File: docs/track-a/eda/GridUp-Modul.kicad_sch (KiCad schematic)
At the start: 47 parts, among them J1 İç ihtiyaç L / N / PE, J2 CT L1, J3 CT L2, J4 CT L3, J5 CT nötr, J6 Genişleme 2×5, J7 RS-485 klemens A / GND / B, J8 SMA panel, J9 Servis USB/UART0, SW1 Reset, U1 ESP32-S3-WROOM-1U-N8, U2 MLX90640ESF-BAA, U3 SHT31-DIS-B, U4 MAX3485, U5 RAC05-05SK/277, U6 LDO 3,3 V ≥600 mA (LD1117S33)

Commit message: İZ A: 03-baglanti-semasi.svg artık KiCad şematiğinden üretiliyor (elle SVG kaldırıldı): sinyal akışına göre yerleşim (CT üst / I²C alt → ESP32 → servis / RS-485 / anten / genişleme; besleme altta), ana hatlar tel (I²C bus, CT merdiveni, UART1↔MAX3485 aynalı), net renk kodu + lejant + blok dolguları, çerçevesiz kırpılmış SVG (2,0 mm etiket ≈ 8 px @1200 px); ERC 0/0, netlist 95 kontrol; 03-pinout ve eda/README güncel
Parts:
- removed C10, C11, C12, C13, C2: 100 nF, symbol Device:C
- removed D1: Schottky (OR), symbol Device:D_Schottky
- removed J7: RS-485 klemens A / GND / B, TerminalBlock_Phoenix:TerminalBlock_Phoenix_MKDS-3-3-5.08_1x03_P5.08mm_Horizontal, symbol Connector_Generic:Conn_01x03
- removed R40: 120 Ω, symbol Device:R
- removed RV1: MOV, symbol Device:Varistor
- removed U6: LDO 3,3 V ≥600 mA (LD1117S33), Package_TO_SOT_SMD:SOT-223-3_TabPin2, symbol Regulator_Linear:LD1117S33TR_SOT223
- added C31: 10 µF, symbol Device:C
- added C32: C_sc süperkap., symbol Device:C_Polarized
- added F1: sigorta, symbol Device:Fuse
- added J1: İç ihtiyaç L / N / PE, TerminalBlock_Phoenix:TerminalBlock_Phoenix_MKDS-3-3-5.08_1x03_P5.08mm_Horizontal, symbol Connector_Generic:Conn_01x03
- added J2: CT L1, TerminalBlock_Phoenix:TerminalBlock_Phoenix_MKDS-3-2-5.08_1x02_P5.08mm_Horizontal, symbol Connector_Generic:Conn_01x02
- added J3: CT L2, TerminalBlock_Phoenix:TerminalBlock_Phoenix_MKDS-3-2-5.08_1x02_P5.08mm_Horizontal, symbol Connector_Generic:Conn_01x02
- added J4: CT L3, TerminalBlock_Phoenix:TerminalBlock_Phoenix_MKDS-3-2-5.08_1x02_P5.08mm_Horizontal, symbol Connector_Generic:Conn_01x02
- added J5: CT nötr, TerminalBlock_Phoenix:TerminalBlock_Phoenix_MKDS-3-2-5.08_1x02_P5.08mm_Horizontal, symbol Connector_Generic:Conn_01x02
- added R52: R_şarj ≈10 Ω, symbol Device:R
- added U4: MAX3485, Package_SO:SOIC-8_3.9x4.9mm_P1.27mm, symbol Interface_UART:MAX3485
- C10: renamed from J2; value CT L1 -> 100 nF; footprint TerminalBlock_Phoenix:TerminalBlock_Phoenix_MKDS-3-2-5.08_1x02_P5.08mm_Horizontal -> (none); symbol Connector_Generic:Conn_01x02 -> Device:C
- C11: renamed from J3; value CT L2 -> 100 nF; footprint TerminalBlock_Phoenix:TerminalBlock_Phoenix_MKDS-3-2-5.08_1x02_P5.08mm_Horizontal -> (none); symbol Connector_Generic:Conn_01x02 -> Device:C
- C12: renamed from J4; value CT L3 -> 100 nF; footprint TerminalBlock_Phoenix:TerminalBlock_Phoenix_MKDS-3-2-5.08_1x02_P5.08mm_Horizontal -> (none); symbol Connector_Generic:Conn_01x02 -> Device:C
- C13: renamed from J5; value CT nötr -> 100 nF; footprint TerminalBlock_Phoenix:TerminalBlock_Phoenix_MKDS-3-2-5.08_1x02_P5.08mm_Horizontal -> (none); symbol Connector_Generic:Conn_01x02 -> Device:C
- C2: renamed from U4; value MAX3485 -> 100 nF; footprint Package_SO:SOIC-8_3.9x4.9mm_P1.27mm -> (none); symbol Interface_UART:MAX3485 -> Device:C
- D1: renamed from R52; value R_şarj ≈10 Ω -> Schottky (OR); symbol Device:R -> Device:D_Schottky
- J7: renamed from J1; value İç ihtiyaç L / N / PE -> RS-485 klemens B / GND / A
- R40: renamed from F1; value sigorta -> 120 Ω; symbol Device:Fuse -> Device:R
- RV1: renamed from C31; value 10 µF -> MOV; symbol Device:C -> Device:Varistor
- U6: renamed from C32; value C_sc süperkap. -> LD1117S33 — 3,3 V, ≥600 mA; footprint (none) -> Package_TO_SOT_SMD:SOT-223-3_TabPin2; symbol Device:C_Polarized -> Regulator_Linear:LD1117S33TR_SOT223
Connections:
- net +3V3: now also C2.1, U6.2 (VO), C31.1, U4.8 (VCC); no longer C2.8 (VCC), RV1.1
- net +5V: now also U6.3 (VI), R52.1
- net 5V_RAW: now also D1.2 (A)
- net CT_L1: now also C10.1
- net CT_L2: now also C11.1
- net CT_L3: now also C12.1
- net CT_N: now also C13.1
- net DE_RE: now also U4.2 (~{RE}), U4.3 (DE); no longer C2.2 (~{RE}), C2.3 (DE)
- net Earth_Protective: now also J1.3 (Pin_3); no longer J7.3 (Pin_3)
- net GND: now also C10.2, C11.2, C12.2, C13.2, C2.2, J7.2 (Pin_2), U6.1 (GND), C31.2, C32.2, U4.5 (GND); no longer C2.5 (GND), RV1.2, U6.2
- net U0RXD: now also J9.2 (Pin_2); no longer J9.4 (Pin_4)
- net U0TXD: now also J9.1 (Pin_1); no longer J9.3 (Pin_3)
- net U1RXD: now also U4.1 (RO); no longer C2.1 (RO)
- net U1TXD: now also U4.4 (DI); no longer C2.4 (DI)
- net USB_DN: now also J9.3 (Pin_3); no longer J9.1 (Pin_1)
- net USB_DP: now also J9.4 (Pin_4); no longer J9.2 (Pin_2)
- net V_BIAS: now also J2.2 (Pin_2), J3.2 (Pin_2), J4.2 (Pin_2), J5.2 (Pin_2); no longer C10.2 (Pin_2), C11.2 (Pin_2), C12.2 (Pin_2), C13.2 (Pin_2)
- net at R40.2: now also J7.3 (Pin_3), U4.6 (A); no longer U5.1 (AC(L))
- net at U5.2 (AC(N)): now also RV1.2, J1.2 (Pin_2); no longer J7.2 (Pin_2)
- net at R10.1, R20.1: now also J2.1 (Pin_1); no longer C10.1 (Pin_1)
- net at R11.1, R21.1: now also J3.1 (Pin_1); no longer C11.1 (Pin_1)
- net at R12.1, R22.1: now also J4.1 (Pin_1); no longer C12.1 (Pin_1)
- net at J7.1 (Pin_1), R40.1: now also U4.7 (B)
- net at R13.1, R23.1: now also J5.1 (Pin_1); no longer C13.1 (Pin_1)
- new net: C32.1, D2.2 (A), R52.2
- new net: F1.1, J1.1 (Pin_1)
- new net: F1.2, RV1.1, U5.1 (AC(L))
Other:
- note added: "2× 4,7 kΩ pull-up → 3V3"
- note added: "3V3"
- note added: "5 V / 230 V"
- note added: "A/B bükümlü çift, ekranlı; son cihazda 2. 120 Ω"
- note added: "Anten — U.FL pigtail → SMA panel → dış anten (pano dış yüzü)"
- note added: "Besleme — 230 V iç ihtiyaç → RAC05 5 V → D1 (OR) → 5 V rayı → LDO 3V3; süperkap R_şarj + D2 yedek; algılama D1 öncesi (§3.4, §7.3)"
- note added: "CT ×4 (analizör yoksa) — burden, V_bias, RC → ADC1"
- note added: "ESP32-S3-WROOM-1U-N8 — Wi-Fi/BLE, U.FL anten"
- note added: "GND / PE"
- note added: "Genişleme 2×5 (boş) — PD / akustik için ayrılmış (§7.1); kör tapa"
- note added: "I²C"
- note added: "I²C — MLX90640 0x33 + SHT31 0x44, tek hat 400 kHz+"
- note added: "KiCad şematik (eda/GridUp-Modul.kicad_sch): ERC 0 hata / 0 uyarı, netlist §3.1 tablosuyla otomatik doğrulanmış. Kavramsal — üretim çizimi değildir (§1.4); pasif değerler tipik."
- note added: "Lejant (tel / etiket rengi) — aynı adlı etiketler aynı nettir; tel kesişmeleri atlama yayıyla gösterilir (bağlantı yok):"
- note added: "Modül bağlantı şeması — ESP32-S3-WROOM-1U etrafında (03-pinout §3.1–3.6)"
- note added: "RS-485 / Modbus RTU — MAX3485, 3,3 V, yarıçift; 120 Ω sonlandırma"
- note added: "U.FL harici anten (1U) — sembolde pin yok, bkz. J8; GPIO10/11 → genişleme (J6)"
- note added: "U.FL pigtail (modül konnektörü) — RF, şemada net değil; mevcut kablo girişinden"
- note added: "UART / RS-485"
- note added: "V_bias = 3V3/2 (CT ön yargı)"
- note added: "analog (CT, algılama)"
- note added: "diğer / bileşen içi"
- note added: "strapping IO0 / IO3 / IO45 / IO46 bağlanmaz; IO35–IO37 flash — kullanılmaz"
- note added: "sıcaklık + nem (ADDR → GND: 0x44)"
- note added: "termal dizi 32×24, 110°×75°, ≤23 mA"
- note added: "→ enerji analizörü (slave 1, akım) / TVOC-2 (slave 2, yalnız trip-diag.)"
- note removed: "Anten — U.FL pigtail → SMA panel konnektörü → dış anten (pano dış yüzü, mevcut kablo girişi)"
- note removed: "Besleme — 230 V iç ihtiyaç devresi → RAC05 5 V → D1 (OR) → 5 V rayı → LDO 3V3; süperkap R_şarj + D2 yedek; algılama D1 öncesinden (03 §3.4, §7.3)"
- note removed: "Genişleme başlığı 2×5 (boş) — PD / akustik için ayrılmış, §7.1 şartı; kutuda kör tapa"
- note removed: "I²C — tek hat, 400 kHz+, 0x33 ≠ 0x44, 2× 4,7 kΩ pull-up → 3V3"
- note removed: "RS-485 / Modbus RTU — MAX3485 sınıfı, 3,3 V, yarıçift yönlü; 120 Ω sonlandırma; A/B bükümlü çift, ekranlı"
- note removed: "Split-core CT ×4 (analizör yoksa) — L1 / L2 / L3 / nötr, her kanal aynı devre: burden + V_bias, 1 kΩ / 100 nF RC → ADC1"
- note removed: "U.FL harici anten (1U) — sembolde pin yok, bkz. J8"
- note removed: "U.FL pigtail (modül konnektörü) — RF, şemada net değil"
- note removed: "V_bias = 3V3/2"
- note removed: "son cihazda 2. 120 Ω sonlandırma"
- note removed: "strapping: IO0 / IO3 / IO45 / IO46 — bağlanmaz; IO35–IO37 flash — kullanılmaz"
- note removed: "sıcaklık + nem, I²C 0x44 (ADDR → GND)"
- note removed: "termal dizi 32×24, 110°×75°, I²C 0x33"
- note removed: "→ enerji analizörü (slave 1, akım) / TVOC-2 (slave 2, yalnız trip-diag. kaydı)"
- note removed: "≤23 mA, 3,3 V"
- moved on the sheet: J7

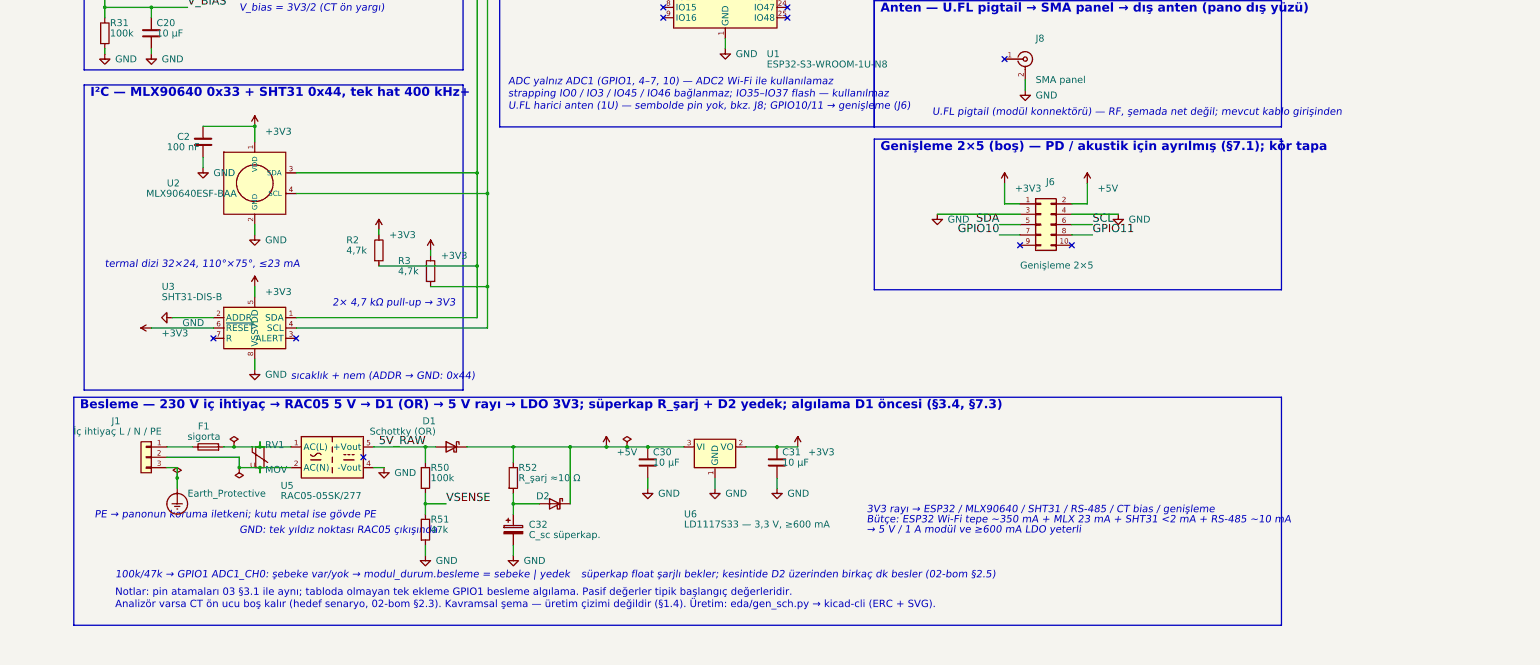
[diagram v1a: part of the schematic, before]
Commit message: İZ A: model/şema datasheet düzeltmeleri — RAC05-05SK/277 31,7 × 26,7 × 21,8 (LDO/D1/D2/bölücü kaydırıldı); süperkap 2× Eaton HV1030-2R7106-R (Ø10,5 × 31,5, 10 F / 2,7 V seri, 10 k dengeleme) + TPS61099 boost 4,6 V → D2 (LD1117 yerine AP7361C-33E düşük dropout); kutu alt yüz rakor sırası PCB klemensleriyle hizalı (RS-485 / SMA / CT / 230 V, PG7 Ø12,5); 02/03/04 SVG'ler, views, f3d/step yeniden üretildi; ERC 0/0, netlist 103 kontrol; README/03-pinout senkron
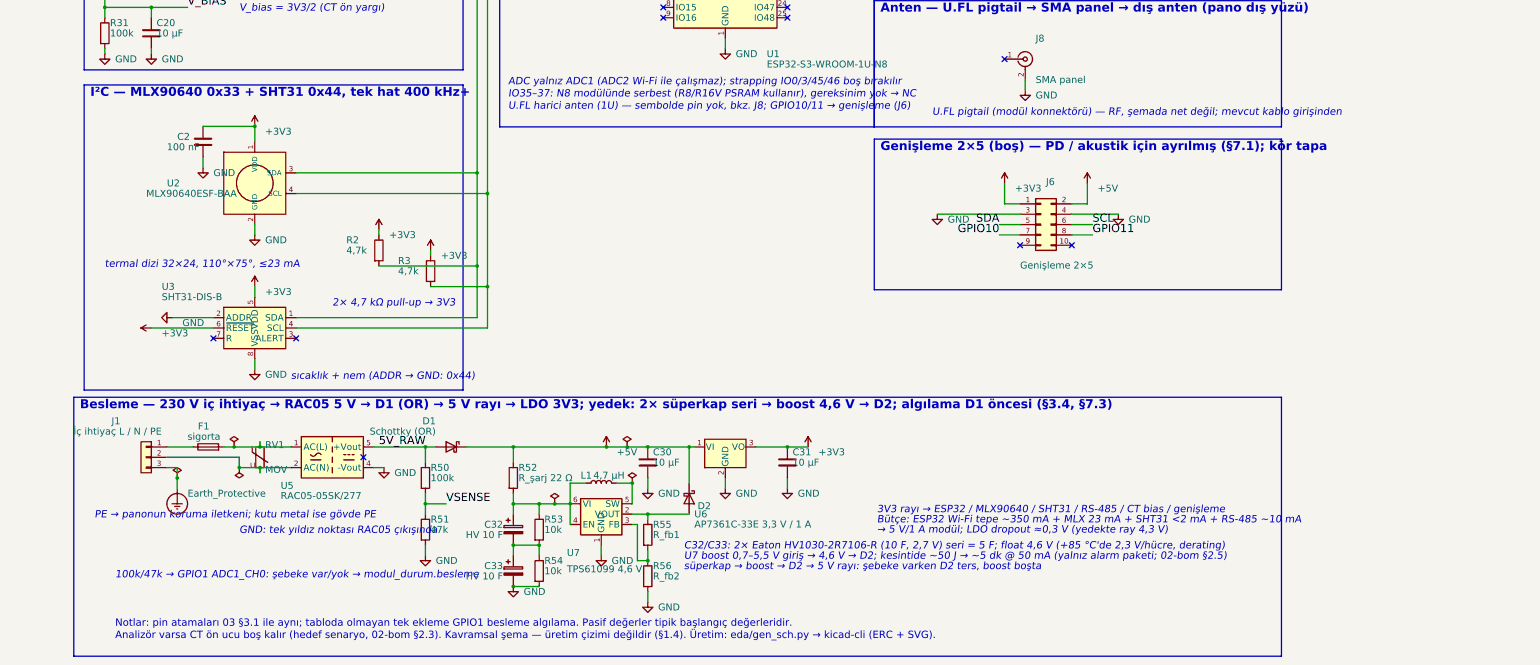
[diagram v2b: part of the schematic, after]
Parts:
- removed C12, C13: 100 nF, symbol Device:C
- removed J5: CT nötr, TerminalBlock_Phoenix:TerminalBlock_Phoenix_MKDS-3-2-5.08_1x02_P5.08mm_Horizontal, symbol Connector_Generic:Conn_01x02
- removed R1: 10k, symbol Device:R
- removed R30: 100k, symbol Device:R
- removed R40: 120 Ω, symbol Device:R
- added C2: 100 nF, symbol Device:C
- added C20: 10 µF, symbol Device:C
- added C33: HV 10 F, symbol Device:C_Polarized
- added J3: CT L2, TerminalBlock_Phoenix:TerminalBlock_Phoenix_MKDS-3-2-5.08_1x02_P5.08mm_Horizontal, symbol Connector_Generic:Conn_01x02
- added L1: 4,7 µH, symbol Device:L
- added R53, R54: 10k, symbol Device:R
- added R55: R_fb1, symbol Device:R
- added R56: R_fb2, symbol Device:R
- added U2: MLX90640ESF-BAA, Package_TO_SOT_THT:TO-39-4, symbol GridUp:MLX90640
- added U3: SHT31-DIS-B, Sensor_Humidity:Sensirion_DFN-8-1EP_2.5x2.5mm_P0.5mm_EP1.1x1.7mm, symbol Sensor_Humidity:SHT31-DIS
- added U6: AP7361C-33E 3,3 V / 1 A, Package_TO_SOT_SMD:SOT-223-3_TabPin2, symbol Regulator_Linear:AP7361C-33E
- added U7: TPS61099 4,6 V, Package_SON:WSON-6-1EP_2x2mm_P0.65mm_EP1x1.6mm, symbol Regulator_Switching:TPS61099DRV
- C12: renamed from C20; value 10 µF -> 100 nF
- C32: value C_sc süperkap. -> HV 10 F
- J1: renamed from U6; value LD1117S33 — 3,3 V, ≥600 mA -> İç ihtiyaç L / N / PE; footprint Package_TO_SOT_SMD:SOT-223-3_TabPin2 -> TerminalBlock_Phoenix:TerminalBlock_Phoenix_MKDS-3-3-5.08_1x03_P5.08mm_Horizontal; symbol Regulator_Linear:LD1117S33TR_SOT223 -> Connector_Generic:Conn_01x03
- J5: renamed from U2; value MLX90640ESF-BAA -> CT nötr; footprint Package_TO_SOT_THT:TO-39-4 -> TerminalBlock_Phoenix:TerminalBlock_Phoenix_MKDS-3-2-5.08_1x02_P5.08mm_Horizontal; symbol GridUp:MLX90640 -> Connector_Generic:Conn_01x02
- R1: renamed from J3; value CT L2 -> 10k; footprint TerminalBlock_Phoenix:TerminalBlock_Phoenix_MKDS-3-2-5.08_1x02_P5.08mm_Horizontal -> (none); symbol Connector_Generic:Conn_01x02 -> Device:R
- R30: renamed from U3; value SHT31-DIS-B -> 100k; footprint Sensor_Humidity:Sensirion_DFN-8-1EP_2.5x2.5mm_P0.5mm_EP1.1x1.7mm -> (none); symbol Sensor_Humidity:SHT31-DIS -> Device:R
- R40: renamed from J1; value İç ihtiyaç L / N / PE -> 120 Ω; footprint TerminalBlock_Phoenix:TerminalBlock_Phoenix_MKDS-3-3-5.08_1x03_P5.08mm_Horizontal -> (none); symbol Connector_Generic:Conn_01x03 -> Device:R
- R52: value R_şarj ≈10 Ω -> R_şarj 22 Ω
- renumbered C2 to C13
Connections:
- net +3V3: now also R1.1, R30.1, C2.1, U2.1 (VDD), U3.5 (VDD), U3.6 (~{RESET}), U6.3 (VO); no longer C13.1, J1.2 (VO), J5.1 (VDD), R30.5 (VDD), R30.6 (~{RESET})
- net +5V: now also U6.1 (VI); no longer J1.3 (VI)
- net CT_L3: now also C12.1
- net CT_N: now also C13.1
- net Earth_Protective: now also J1.3 (Pin_3); no longer R40.3 (Pin_3)
- net GND: now also C2.2, C20.2, C33.2, R54.2, R56.2, U2.2 (GND), U3.2 (ADDR), U3.8 (VSS), U3.9 (VSS), U6.2 (GND), U7.1 (GND), U7.7 (GND); no longer C32.2, J1.1 (GND), J5.2 (GND), R30.2 (ADDR), R30.8 (VSS), R30.9 (VSS)
- net SCL: now also U2.4 (SCL), U3.4 (SCL); no longer J5.4 (SCL), R30.4 (SCL)
- net SDA: now also U2.3 (SDA), U3.1 (SDA); no longer J5.3 (SDA), R30.1 (SDA)
- net V_BIAS: now also J5.2 (Pin_2), R30.2, C20.1, J3.2 (Pin_2); no longer C12.1, R1.2 (Pin_2)
- net at R13.1, R23.1: now also J5.1 (Pin_1)
- net at C1.1, SW1.2, U1.3 (EN): now also R1.2
- net at C32.1, R52.2: now also L1.1, R53.1, U7.4 (EN), U7.6 (VI); no longer D2.2 (A)
- net at J7.1 (Pin_1), U4.7 (B): now also R40.1
- net at J7.3 (Pin_3), U4.6 (A): now also R40.2
- net at F1.1: now also J1.1 (Pin_1); no longer R40.1 (Pin_1)
- net at RV1.2, U5.2 (AC(N)): now also J1.2 (Pin_2); no longer R40.2 (Pin_2)
- net at R11.1, R21.1: now also J3.1 (Pin_1); no longer R1.1 (Pin_1)
- new net: D2.2 (A), R55.1, U7.2 (VOUT)
- new net: R55.2, R56.1, U7.3 (FB)
- new net: C32.2, C33.1, R53.2, R54.1
- new net: L1.2, U7.5 (SW)
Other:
- note added: "100k/47k → GPIO1 ADC1_CH0: şebeke var/yok → modul_durum.besleme"
- note added: "ADC yalnız ADC1 (ADC2 Wi-Fi ile çalışmaz); strapping IO0/3/45/46 boş bırakılır"
- note added: "Besleme — 230 V iç ihtiyaç → RAC05 5 V → D1 (OR) → 5 V rayı → LDO 3V3; yedek: 2× süperkap seri → boost 4,6 V → D2; algılama D1 öncesi (§3.4, §7.3)"
- note added: "C32/C33: 2× Eaton HV1030-2R7106-R (10 F, 2,7 V) seri = 5 F; float 4,6 V (+85 °C'de 2,3 V/hücre, derating)"
- note added: "IO35–37: N8 modülünde serbest (R8/R16V PSRAM kullanır), gereksinim yok → NC"
- note added: "U7 boost 0,7–5,5 V giriş → 4,6 V → D2; kesintide ~50 J → ~5 dk @ 50 mA (yalnız alarm paketi; 02-bom §2.5)"
- note added: "süperkap → boost → D2 → 5 V rayı: şebeke varken D2 ters, boost boşta"
- note added: "→ 5 V/1 A modül; LDO dropout ≈0,3 V (yedekte ray 4,3 V)"
- note removed: "100k/47k → GPIO1 ADC1_CH0: şebeke var/yok → modul_durum.besleme = sebeke | yedek"
- note removed: "ADC yalnız ADC1 (GPIO1, 4–7, 10) — ADC2 Wi-Fi ile kullanılamaz"
- note removed: "Besleme — 230 V iç ihtiyaç → RAC05 5 V → D1 (OR) → 5 V rayı → LDO 3V3; süperkap R_şarj + D2 yedek; algılama D1 öncesi (§3.4, §7.3)"
- note removed: "strapping IO0 / IO3 / IO45 / IO46 bağlanmaz; IO35–IO37 flash — kullanılmaz"
- note removed: "süperkap float şarjlı bekler; kesintide D2 üzerinden birkaç dk besler (02-bom §2.5)"
- note removed: "→ 5 V / 1 A modül ve ≥600 mA LDO yeterli"
- moved on the sheet: C12, C13, J1

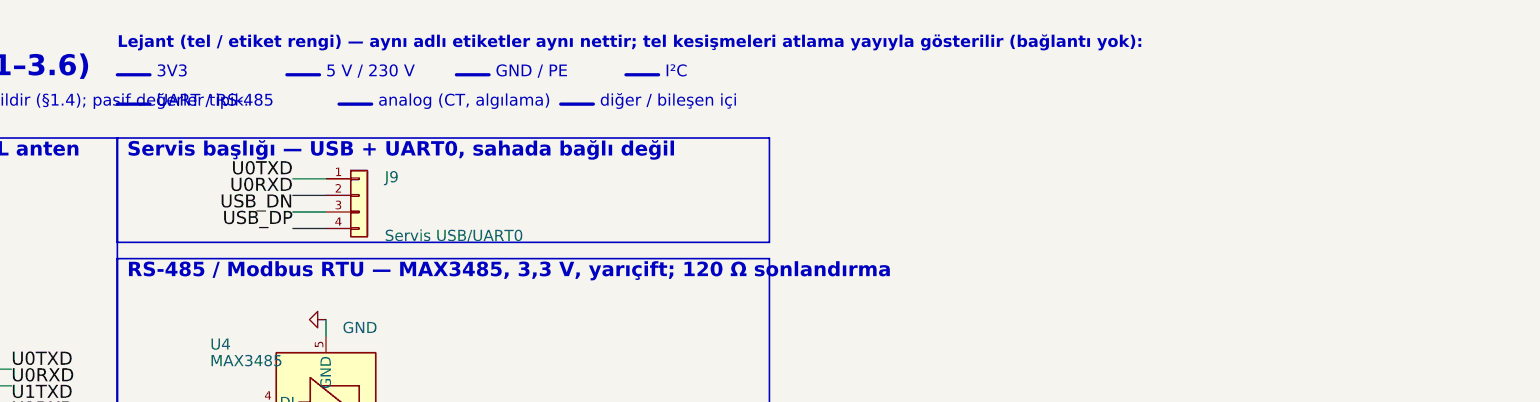
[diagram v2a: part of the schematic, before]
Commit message: İZ A: 03 şema — lejant başlığı iki satıra bölündü (viewBox sağ sınırını 13 mm aşıyordu), RS-485 blok başlığı kısaltıldı; tüm metinler Arial metriğiyle ölçüldü, taşma 0 (en yakın 3,1 mm içeride)
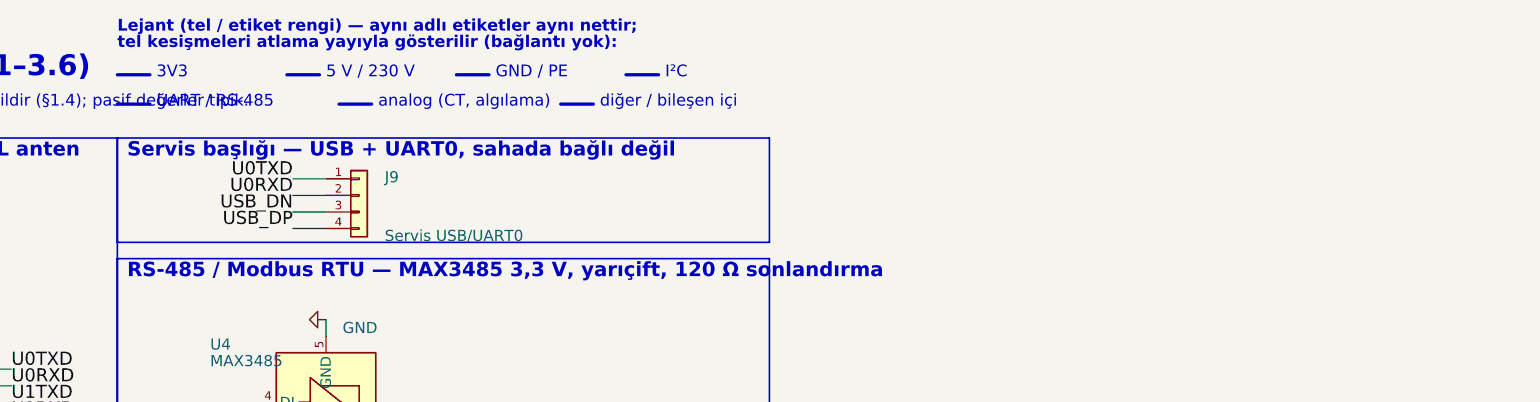
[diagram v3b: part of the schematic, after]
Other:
- note added: "Lejant (tel / etiket rengi) — aynı adlı etiketler aynı nettir;"
- note added: "RS-485 / Modbus RTU — MAX3485 3,3 V, yarıçift, 120 Ω sonlandırma"
- note added: "tel kesişmeleri atlama yayıyla gösterilir (bağlantı yok):"
- note removed: "Lejant (tel / etiket rengi) — aynı adlı etiketler aynı nettir; tel kesişmeleri atlama yayıyla gösterilir (bağlantı yok):"
- note removed: "RS-485 / Modbus RTU — MAX3485, 3,3 V, yarıçift; 120 Ω sonlandırma"
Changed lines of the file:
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@@
 		)
 	)
-	(text "Lejant (tel / etiket rengi) — aynı adlı etiketler aynı nettir; tel kesişmeleri atlama yayıyla gösterilir (bağlantı yok):"
+	(text "Lejant (tel / etiket rengi) — aynı adlı etiketler aynı nettir;"
+		(exclude_from_sim no)
+		(at 222 26 0)
+		(effects
+			(font
+				(size 1.8 1.8)
+				(bold yes)
+			)
+			(justify left bottom)
+		)
+	)
+	(text "tel kesişmeleri atlama yayıyla gösterilir (bağlantı yok):"
 		(exclude_from_sim no)
 		(at 222 28.5 0)
@@
 		)
 	)
-	(text "RS-485 / Modbus RTU — MAX3485, 3,3 V, yarıçift; 120 Ω sonlandırma"
+	(text "RS-485 / Modbus RTU — MAX3485 3,3 V, yarıçift, 120 Ω sonlandırma"
 		(exclude_from_sim no)
 		(at 223.5 63.7 0)

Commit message: İZ A: 03 şema — TPS61099 bobini L1 4,7 → 2,2 µH (datasheet §7.3: 0,7 / 2,2 / 2,86 µH; 4,7 spesifikasyon dışıydı); şema, netlist ve SVG yeniden üretildi, ERC 0/0, netlist 103/103, metin taşması 0
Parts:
- L1: value 4,7 µH -> 2,2 µH
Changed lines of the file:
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@@
 			)
 		)
-		(property "Value" "4,7 µH"
+		(property "Value" "2,2 µH"
 			(at 153 235.6 270)
 			(effects
